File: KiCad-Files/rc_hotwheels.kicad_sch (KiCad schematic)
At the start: 5 parts, among them IC1 BD6211F-E2, M1 Motor_DC, U1 STM32F070F6P6, U2 NRF24L01_Breakout

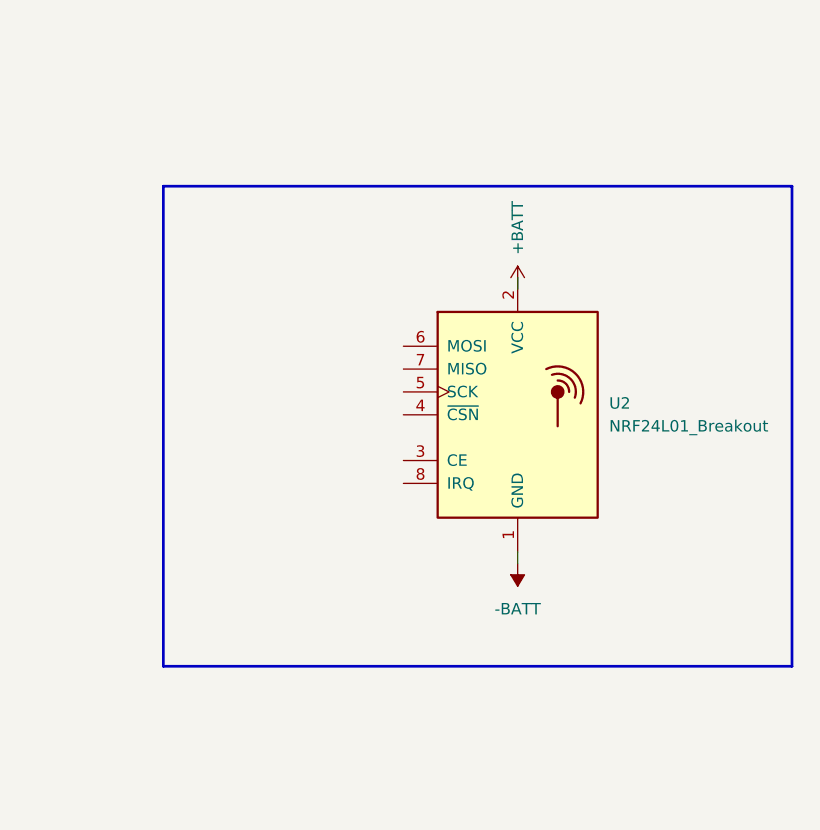
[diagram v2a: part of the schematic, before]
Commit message: Updated the nRF24L01 connection to the MCU.
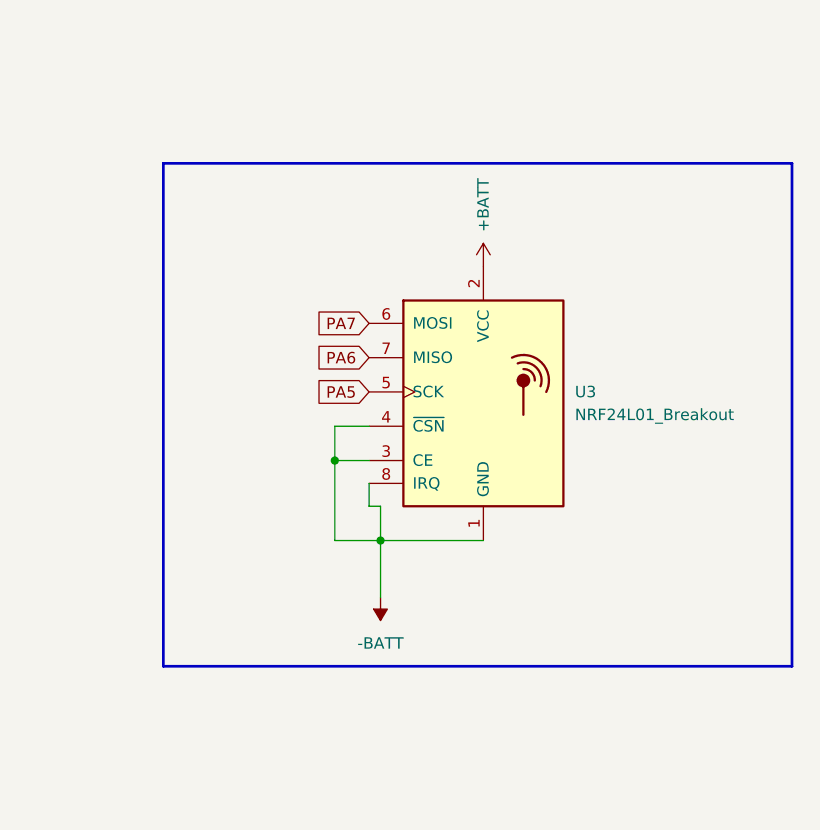
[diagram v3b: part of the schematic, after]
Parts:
- removed U2: NRF24L01_Breakout, RF_Module:nRF24L01_Breakout, symbol RF:NRF24L01_Breakout
- added U3: NRF24L01_Breakout, RF_Module:nRF24L01_Breakout, symbol RF:NRF24L01_Breakout
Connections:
- net +BATT: now also U3.2 (VCC)
- net -BATT: now also U3.1 (GND), U3.3 (CE), U3.4 (~{CSN}), U3.8 (IRQ)
- new net PA5: U3.5 (SCK)
- new net PA6: U3.7 (MISO)
- new net PA7: U3.6 (MOSI)
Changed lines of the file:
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@@
 (kicad_sch (version 20230121) (generator eeschema)
   (paper "A4")
+  (junction (at 231.14 140.97) (diameter 0) (color 0 0 0 0)
+  )
+  (junction (at 236.22 149.86) (diameter 0) (color 0 0 0 0)
+  )
   (junction (at 74.93 39.37) (diameter 0) (color 0 0 0 0)
   )
@@
     (stroke (width 0) (type default))
   )
+  (wire (pts (xy 234.95 146.05) (xy 236.22 146.05))
+    (stroke (width 0) (type default))
+  )
   (wire (pts (xy 40.64 172.72) (xy 40.64 157.48))
     (stroke (width 0) (type default))
@@
     (stroke (width 0) (type default))
   )
+  (wire (pts (xy 231.14 140.97) (xy 231.14 149.86))
+    (stroke (width 0) (type default))
+  )
+  (wire (pts (xy 234.95 140.97) (xy 231.14 140.97))
+    (stroke (width 0) (type default))
+  )
   (wire (pts (xy 74.93 25.4) (xy 74.93 29.21))
     (stroke (width 0) (type default))
@@
     (stroke (width 0) (type default))
   )
-  (wire (pts (xy 251.46 151.13) (xy 251.46 152.4))
+  (wire (pts (xy 236.22 146.05) (xy 236.22 149.86))
+    (stroke (width 0) (type default))
+  )
+  (wire (pts (xy 236.22 149.86) (xy 236.22 156.21))
     (stroke (width 0) (type default))
   )
@@
     (stroke (width 0) (type default))
   )
+  (wire (pts (xy 234.95 137.16) (xy 231.14 137.16))
+    (stroke (width 0) (type default))
+  )
   (wire (pts (xy 40.64 157.48) (xy 49.53 157.48))
     (stroke (width 0) (type default))
   )
-  (wire (pts (xy 251.46 120.65) (xy 251.46 121.92))
+  (wire (pts (xy 231.14 149.86) (xy 236.22 149.86))
+    (stroke (width 0) (type default))
+  )
+  (wire (pts (xy 234.95 143.51) (xy 234.95 146.05))
     (stroke (width 0) (type default))
   )
@@
     (stroke (width 0) (type default))
   )
+  (wire (pts (xy 231.14 137.16) (xy 231.14 140.97))
+    (stroke (width 0) (type default))
+  )
+  (wire (pts (xy 236.22 149.86) (xy 247.65 149.86))
+    (stroke (width 0) (type default))
+  )
   (wire (pts (xy 30.48 160.02) (xy 30.48 176.53))
     (stroke (width 0) (type default))
   )
-  (rectangle (start 212.09 110.49) (end 281.94 163.83)
+  (rectangle (start 212.09 107.95) (end 281.94 163.83)
     (stroke (width 0.3) (type solid) (color 0 0 0 1))
     (fill (type none))
@@
     (effects (font (size 1.27 1.27)) (justify left top))
   )
+  (global_label "PA7" (shape input) (at 234.95 125.73 180) (fields_autoplaced)
+    (effects (font (size 1.27 1.27)) (justify right))
+    (property "Intersheetrefs" "${INTERSHEET_REFS}" (at 228.3967 125.73 0)
+      (effects (font (size 1.27 1.27)) (justify right) hide)
+    )
+  )
+  (global_label "PA6" (shape input) (at 234.95 129.54 180) (fields_autoplaced)
+    (effects (font (size 1.27 1.27)) (justify right))
+    (property "Intersheetrefs" "${INTERSHEET_REFS}" (at 228.3967 129.54 0)
+      (effects (font (size 1.27 1.27)) (justify right) hide)
+    )
+  )
+  (global_label "PA5" (shape input) (at 234.95 133.35 180) (fields_autoplaced)
+    (effects (font (size 1.27 1.27)) (justify right))
+    (property "Intersheetrefs" "${INTERSHEET_REFS}" (at 228.3967 133.35 0)
+      (effects (font (size 1.27 1.27)) (justify right) hide)
+    )
+  )
+  (symbol (lib_name "NRF24L01_Breakout_1") (lib_id "RF:NRF24L01_Breakout") (at 247.65 134.62 0) (unit 1)
+    (in_bom yes) (on_board yes) (dnp no) (fields_autoplaced)
+    (property "Reference" "U3" (at 257.81 133.35 0)
+      (effects (font (size 1.27 1.27)) (justify left))
+    )
+    (property "Value" "NRF24L01_Breakout" (at 257.81 135.89 0)
+      (effects (font (size 1.27 1.27)) (justify left))
+    )
+    (property "Footprint" "RF_Module:nRF24L01_Breakout" (at 251.46 119.38 0)
+      (effects (font (size 1.27 1.27) italic) (justify left) hide)
+    )
+    (property "Datasheet" "http://www.nordicsemi.com/eng/content/download/2730/34105/file/nRF24L01_Product_Specification_v2_0.pdf" (at 247.65 137.16 0)
+      (effects (font (size 1.27 1.27)) hide)
+    )
+    (pin "1")
+    (pin "2")
+    (pin "3")
+    (pin "4")
+    (pin "5")
+    (pin "6")
+    (pin "7")
+    (pin "8")
+    (instances
+      (project "rc_hotwheels"
+        (path "/0b835094-f9c0-45ab-a312-d1f27d043c8e"
+          (reference "U3") (unit 1)
+        )
+      )
+    )
+  )
   (symbol (lib_id "power:+BATT") (at 77.47 44.45 270) (unit 1)
     (in_bom yes) (on_board yes) (dnp no)
@@
     )
   )
-  (symbol (lib_id "power:+BATT") (at 251.46 121.92 0) (unit 1)
+  (symbol (lib_id "power:+BATT") (at 247.65 119.38 0) (unit 1)
     (in_bom yes) (on_board yes) (dnp no)
-    (property "Reference" "#PWR06" (at 251.46 125.73 0)
-      (effects (font (size 1.27 1.27)) hide)
-    )
-    (property "Value" "+BATT" (at 251.46 118.11 90)
-      (effects (font (size 1.27 1.27)) (justify left))
-    )
-    (property "Footprint" "" (at 251.46 121.92 0)
-      (effects (font (size 1.27 1.27)) hide)
-    )
-    (property "Datasheet" "" (at 251.46 121.92 0)
+    (property "Reference" "#PWR06" (at 247.65 123.19 0)
+      (effects (font (size 1.27 1.27)) hide)
+    )
+    (property "Value" "+BATT" (at 247.65 115.57 90)
+      (effects (font (size 1.27 1.27)) (justify left))
+    )
+    (property "Footprint" "" (at 247.65 119.38 0)
+      (effects (font (size 1.27 1.27)) hide)
+    )
+    (property "Datasheet" "" (at 247.65 119.38 0)
       (effects (font (size 1.27 1.27)) hide)
     )
@@
     )
   )
-  (symbol (lib_id "RF:NRF24L01_Breakout") (at 251.46 135.89 0) (unit 1)
-    (in_bom yes) (on_board yes) (dnp no) (fields_autoplaced)
-    (property "Reference" "U2" (at 261.62 134.62 0)
-      (effects (font (size 1.27 1.27)) (justify left))
-    )
-    (property "Value" "NRF24L01_Breakout" (at 261.62 137.16 0)
-      (effects (font (size 1.27 1.27)) (justify left))
-    )
-    (property "Footprint" "RF_Module:nRF24L01_Breakout" (at 255.27 120.65 0)
-      (effects (font (size 1.27 1.27) italic) (justify left) hide)
-    )
-    (property "Datasheet" "http://www.nordicsemi.com/eng/content/download/2730/34105/file/nRF24L01_Product_Specification_v2_0.pdf" (at 251.46 138.43 0)
-      (effects (font (size 1.27 1.27)) hide)
-    )
-    (pin "1")
-    (pin "2")
-    (pin "3")
-    (pin "4")
-    (pin "5")
-    (pin "6")
-    (pin "7")
-    (pin "8")
-    (instances
-      (project "rc_hotwheels"
-        (path "/0b835094-f9c0-45ab-a312-d1f27d043c8e"
-          (reference "U2") (unit 1)
-        )
-      )
-    )
-  )
-  (symbol (lib_id "power:-BATT") (at 251.46 152.4 180) (unit 1)
-    (in_bom yes) (on_board yes) (dnp no) (fields_autoplaced)
-    (property "Reference" "#PWR07" (at 251.46 148.59 0)
-      (effects (font (size 1.27 1.27)) hide)
-    )
-    (property "Value" "-BATT" (at 251.46 157.48 0)
+  (symbol (lib_id "power:-BATT") (at 236.22 156.21 180) (unit 1)
+    (in_bom yes) (on_board yes) (dnp no) (fields_autoplaced)
+    (property "Reference" "#PWR07" (at 236.22 152.4 0)
+      (effects (font (size 1.27 1.27)) hide)
+    )
+    (property "Value" "-BATT" (at 236.22 161.29 0)
       (effects (font (size 1.27 1.27)))
     )
-    (property "Footprint" "" (at 251.46 152.4 0)
-      (effects (font (size 1.27 1.27)) hide)
-    )
-    (property "Datasheet" "" (at 251.46 152.4 0)
-      (effects (font (size 1.27 1.27)) hide)
-    )
+    (property "Footprint" "" (at 236.22 156.21 0)
+      (effects (font (size 1.27 1.27)) hide)
+    )
+    (property "Datasheet" "" (at 236.22 156.21 0)
+      (effects (font (size 1.27 1.27)) hide)
+    )

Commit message: Servo motor
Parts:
- added S_M1: Linear_Servo_Motor, symbol Motor:Motor_Servo
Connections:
- net +BATT: now also S_M1.2 (+)
- net -BATT: now also S_M1.3 (-)
- new net PA9: S_M1.1 (PWM)
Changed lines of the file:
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@@
+    (stroke (width 0) (type default))
+  )
+  (wire (pts (xy 27.94 71.12) (xy 30.48 71.12))
     (stroke (width 0) (type default))
   )
@@
   (wire (pts (xy 30.48 160.02) (xy 30.48 176.53))
     (stroke (width 0) (type default))
+  )
+  (rectangle (start 15.24 58.42) (end 71.12 81.28)
+    (stroke (width 0.3) (type default) (color 0 0 0 1))
+    (fill (type none))
   )
   (rectangle (start 212.09 107.95) (end 281.94 163.83)
@@
     (fill (type none))
   )
+  (text_box "Linear servo motor"
+    (at 43.18 62.23 0) (size 24.13 3.81)
+    (stroke (width 0) (type default))
+    (fill (type none))
+    (effects (font (size 1.27 1.27)) (justify left top))
+  )
   (text_box "Power of microcontroller"
     (at 20.32 19.05 0) (size 17.78 5.08)
@@
     (fill (type none))
     (effects (font (size 1.27 1.27)) (justify left top))
+  )
+  (global_label "PA9" (shape input) (at 27.94 71.12 180) (fields_autoplaced)
+    (effects (font (size 1.27 1.27)) (justify right))
+    (property "Intersheetrefs" "${INTERSHEET_REFS}" (at 21.4661 71.12 0)
+      (effects (font (size 1.27 1.27)) (justify right) hide)
+    )
   )
   (global_label "PA7" (shape input) (at 234.95 125.73 180) (fields_autoplaced)
@@
     (property "Intersheetrefs" "${INTERSHEET_REFS}" (at 228.3967 133.35 0)
       (effects (font (size 1.27 1.27)) (justify right) hide)
+    )
+  )
+  (symbol (lib_id "power:-BATT") (at 30.48 76.2 90) (unit 1)
+    (in_bom yes) (on_board yes) (dnp no) (fields_autoplaced)
+    (property "Reference" "#PWR010" (at 34.29 76.2 0)
+      (effects (font (size 1.27 1.27)) hide)
+    )
+    (property "Value" "-BATT" (at 26.67 76.2 90)
+      (effects (font (size 1.27 1.27)) (justify left))
+    )
+    (property "Footprint" "" (at 30.48 76.2 0)
+      (effects (font (size 1.27 1.27)) hide)
+    )
+    (property "Datasheet" "" (at 30.48 76.2 0)
+      (effects (font (size 1.27 1.27)) hide)
+    )
+    (pin "1")
+    (instances
+      (project "rc_hotwheels"
+        (path "/0b835094-f9c0-45ab-a312-d1f27d043c8e"
+          (reference "#PWR010") (unit 1)
+        )
+      )
     )
   )
@@
     )
   )
+  (symbol (lib_id "power:+BATT") (at 30.48 73.66 90) (unit 1)
+    (in_bom yes) (on_board yes) (dnp no)
+    (property "Reference" "#PWR09" (at 34.29 73.66 0)
+      (effects (font (size 1.27 1.27)) hide)
+    )
+    (property "Value" "+BATT" (at 26.67 73.66 90)
+      (effects (font (size 1.27 1.27)) (justify left))
+    )
+    (property "Footprint" "" (at 30.48 73.66 0)
+      (effects (font (size 1.27 1.27)) hide)
+    )
+    (property "Datasheet" "" (at 30.48 73.66 0)
+      (effects (font (size 1.27 1.27)) hide)
+    )
+    (pin "1")
+    (instances
+      (project "rc_hotwheels"
+        (path "/0b835094-f9c0-45ab-a312-d1f27d043c8e"
+          (reference "#PWR09") (unit 1)
+        )
+      )
+    )
+  )
   (symbol (lib_id "SamacSys_Parts:BD6211F-E2") (at 40.64 172.72 0) (unit 1)
     (in_bom yes) (on_board yes) (dnp no) (fields_autoplaced)
@@
         )
       )
+    )
+  )
+  (symbol (lib_id "Motor:Motor_Servo") (at 38.1 74.93 0) (unit 1)
+    (in_bom yes) (on_board yes) (dnp no) (fields_autoplaced)
+    (property "Reference" "S_M1" (at 40.64 72.39 0)
+      (effects (font (size 1.27 1.27)) (justify left))
+    )
+    (property "Value" "Linear_Servo_Motor" (at 40.64 74.93 0)
+      (effects (font (size 1.27 1.27)) (justify left))
+    )
+    (property "Footprint" "" (at 38.1 78.486 0)
+      (effects (font (size 1.27 1.27)) hide)
+    )
+    (property "Datasheet" "" (at 38.1 78.486 0)
+      (effects (font (size 1.27 1.27)) hide)
+    )
+    (pin "1")
+    (pin "2")
+    (pin "3")
+    (instances
+      (project "rc_hotwheels"
+        (path "/0b835094-f9c0-45ab-a312-d1f27d043c8e"
+          (reference "S_M1") (unit 1)
+        )
+      )
